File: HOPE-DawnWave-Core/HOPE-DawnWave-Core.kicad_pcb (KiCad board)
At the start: 2 copper layers, 50 parts, among them J1 USB_C_Receptacle_USB2.0_16P, J2 Screw_Terminal_01x02, SW1 RST, SW2 BOOT, U1 TLV62569DRL, U2 USBLC6-2P6, U3 ESP32-C6-WROOM-1, U4 MAX98357A, U5 BME688, X1 EYE_SPI_DISPLAY_FLIP

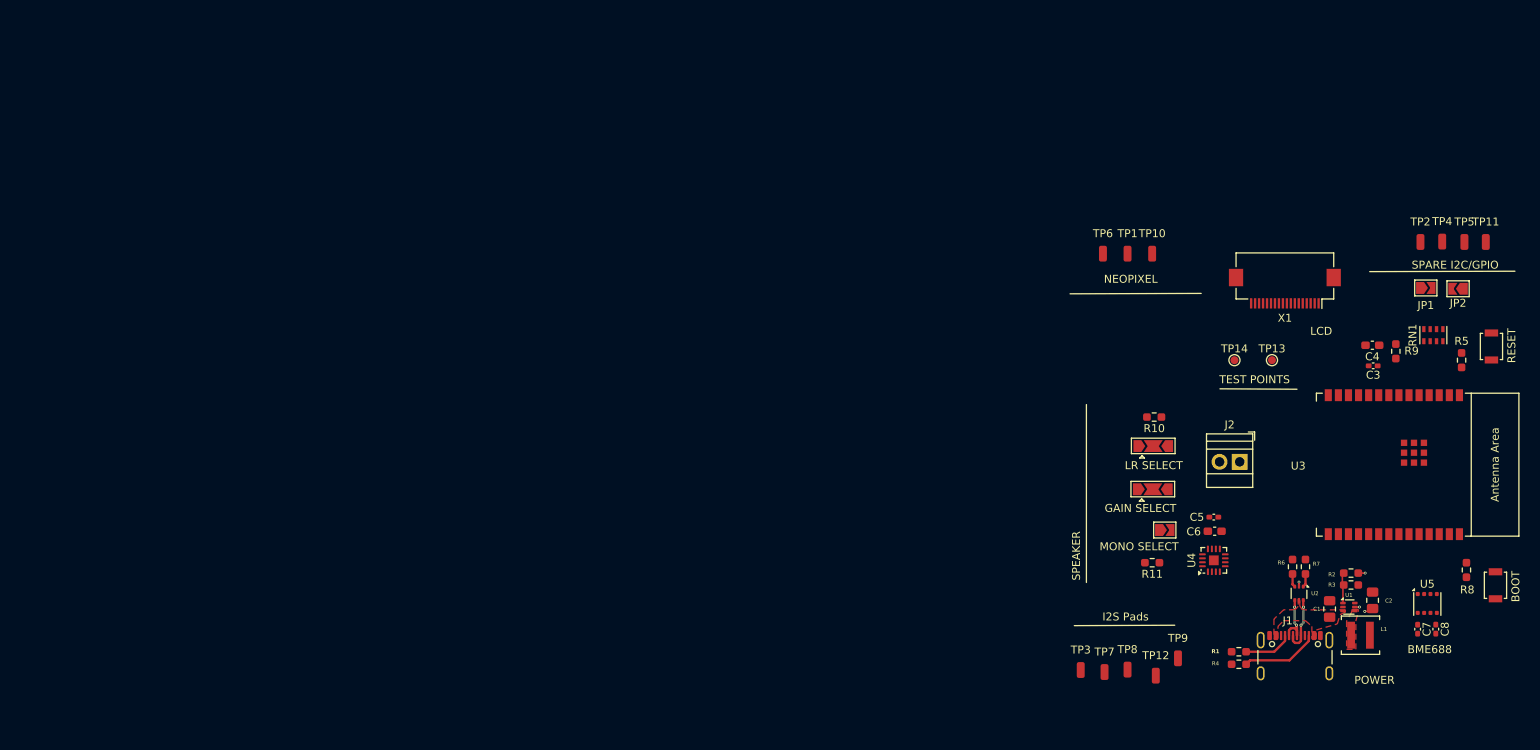
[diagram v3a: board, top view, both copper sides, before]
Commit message: fixed gitignore and completed major component placement iteration
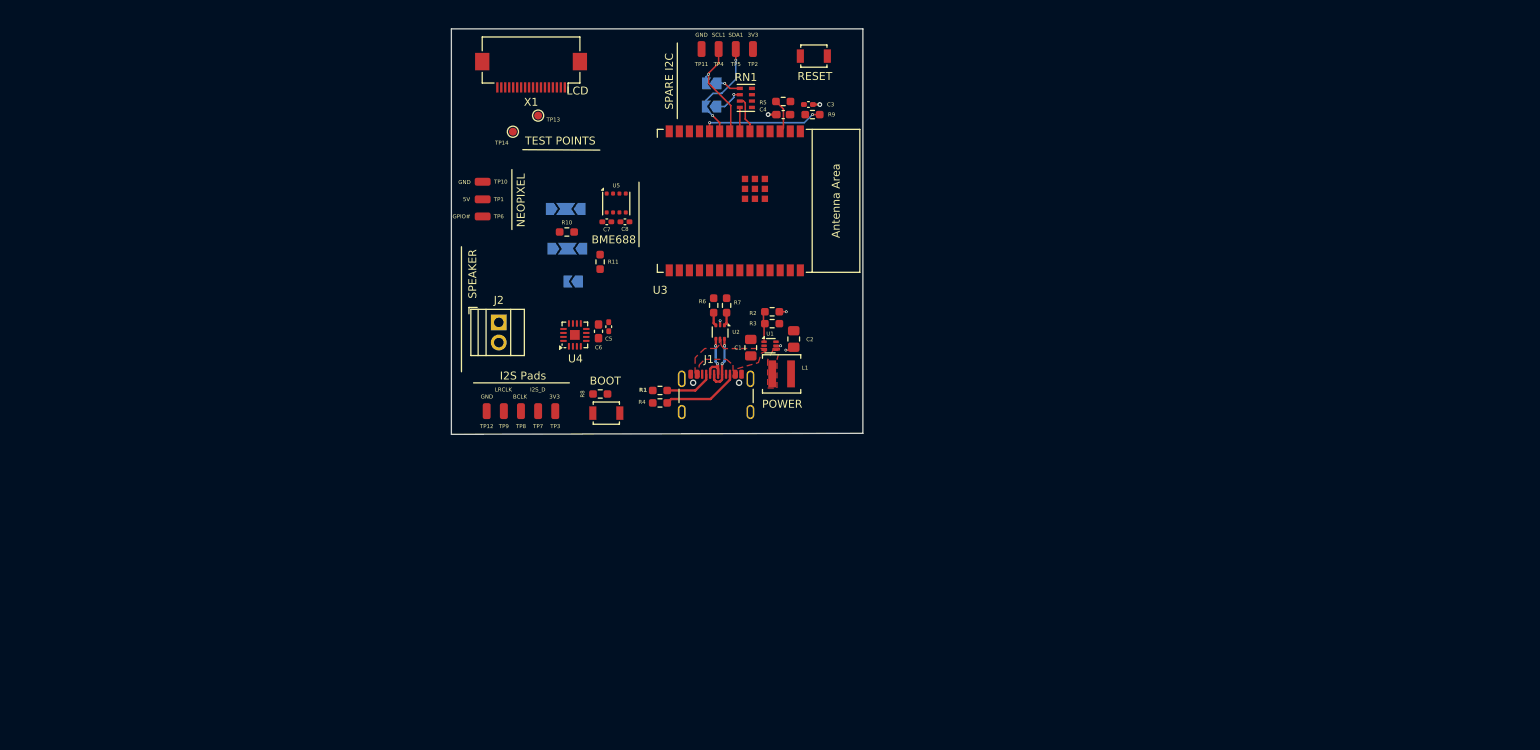
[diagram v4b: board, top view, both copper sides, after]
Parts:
- JP1, JP2, JP3, JP4, JP5: moved to B.Cu
- moved C7 114.3 mm to (142.7, 91.0), turned to 0 degrees
- moved C8 114.3 mm to (144.9, 91.0), turned to 0 degrees
- moved SW2 114.0 mm to (142.6, 115.1), turned to 180 degrees
- moved U5 113.9 mm to (143.8, 88.7)
- moved R8 111.3 mm to (141.8, 112.7), turned to 180 degrees
- moved TP11 101.7 mm to (154.6, 69.3)
- moved X1 98.7 mm to (133.1, 72.3)
- moved TP13 97.4 mm to (134.0, 77.7)
- moved JP2 96.8 mm to (155.9, 76.5)
- moved TP14 95.3 mm to (130.8, 79.7)
- moved J2 94.9 mm to (129.1, 103.7), turned to -90 degrees
- moved TP5 94.9 mm to (158.9, 69.3)
- moved TP4 94.3 mm to (156.7, 69.3)
- moved JP1 93.5 mm to (155.9, 73.6), turned to 180 degrees
- moved SW1 92.8 mm to (168.7, 70.2), turned to 180 degrees
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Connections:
- U3 pad 6: MCU_SDA0 -> MCU_SCL0
- U3 pad 7: MCU_SCL0 -> MCU_SDA0
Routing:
- net Net-(U3-GPIO8): track 0.00 -> 15.4 mm, vias 0 -> 2
- net MCU_SCL1: track 0.00 -> 13.4 mm, vias 0 -> 1
- net MCU_SDA1: track 0.00 -> 13.3 mm, vias 0 -> 2
- net MCU_SCL0: track 0.00 -> 4.60 mm
- net /MCU_EN: track 0.00 -> 4.32 mm
- net Net-(JP2-A): track 0.00 -> 3.70 mm, vias 0 -> 1
- net Net-(JP1-A): track 0.00 -> 3.42 mm, vias 0 -> 1
- net MCU_SDA0: track 0.00 -> 3.01 mm
- net GND: track 0.50 -> 2.41 mm, vias 1 -> 3
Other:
- board outline added: 51.8 x 51.1 mm
- board text added: "3V3"
- board text added: "5V"
- board text added: "BCLK"
- board text added: "GND"
- board text added: "GPIO#"
- board text added: "I2S_D"
- board text added: "LRCLK"
- board text added: "SCL1"
- board text added: "SDA1"
- board text added: "SPARE I2C"
- board text removed: "SPARE I2C/GPIO"

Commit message: big progress oops
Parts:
- moved SW1 37.4 mm to (165.9, 107.4)
- moved R5 29.0 mm to (165.1, 104.9), turned to 0 degrees
- moved R8 23.1 mm to (164.9, 112.8)
- moved SW2 23.1 mm to (165.7, 115.2)
- moved JP4 11.5 mm to (129.9, 98.0)
- moved R1 10.7 mm to (159.3, 116.3), turned to 0 degrees
- moved JP5 10.2 mm to (129.5, 93.5)
- moved JP3 10.2 mm to (128.8, 89.4)
- moved R10 10.2 mm to (128.7, 87.3)
- moved R4 9.97 mm to (159.3, 114.8), turned to 0 degrees
- moved TP1 9.85 mm to (126.7, 98.0)
- moved R11 8.54 mm to (133.9, 93.0)
- moved TP13 8.06 mm to (134.0, 85.7)
- moved U5 7.83 mm to (136.0, 88.9), turned to 90 degrees
- moved C8 7.32 mm to (138.4, 87.8), turned to 90 degrees
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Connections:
- U3 pad 11: MCU_DRST -> MCU_TD
- U3 pad 12: MCU_TD -> MCU_BACKLIGHT
- U3 pad 16: MCU_MISO -> MCU_LRCLK
- U3 pad 17: MCU_SCLK -> MCU_BCLK
- U3 pad 18: MCU_MOSI -> MCU_I2S_D
- U3 pad 19: MCU_D/C -> GPIO_NP
- U3 pad 23: MCU_BACKLIGHT -> MCU_DRST
- U3 pad 24: MCU_LRCLK -> MCU_MISO
- U3 pad 25: MCU_BCLK -> MCU_SCLK
- U3 pad 26: MCU_I2S_D -> MCU_MOSI
- U3 pad 27: GPIO_NP -> MCU_D/C
- U3 pad 6: MCU_SCL0 -> MCU_SDA0
- U3 pad 7: MCU_SDA0 -> MCU_SCL0
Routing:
- net MCU_SDA0: track 3.01 -> 41.4 mm
- net MCU_SCL0: track 4.60 -> 40.1 mm
- net /MCU_BOOT: track 0.00 -> 32.2 mm
- net MCU_LRCLK: track 0.00 -> 30.9 mm, vias 0 -> 2
- net MCU_BCLK: track 0.00 -> 30.7 mm, vias 0 -> 2
- net /MCU_USB_D-: track 0.00 -> 30.5 mm, vias 0 -> 2
- net MCU_I2S_D: track 0.00 -> 30.0 mm, vias 0 -> 2
- net /MCU_USB_D+: track 0.00 -> 28.9 mm, vias 0 -> 2
- net MCU_TD: track 0.00 -> 25.5 mm
- net GPIO_NP: track 0.00 -> 24.7 mm
- net /MCU_EN: track 4.32 -> 28.1 mm
- net MCU_BACKLIGHT: track 0.00 -> 14.7 mm
- net VBUS: track 0.58 -> 9.51 mm, vias 1 -> 2
- net GND: track 2.41 -> 11.1 mm, vias 3 -> 9
- net +3.3V: track 2.01 -> 9.55 mm, vias 2 -> 10
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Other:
- board size 51.8 x 51.1 mm -> 44.6 x 48 mm
- board text added: "+"
- board text added: "-"
- board text added: "SCL0"
- board text added: "SCL1_PU"
- board text added: "SDA0"
- board text added: "SDA1_PU"
- board text removed: "TEST POINTS"

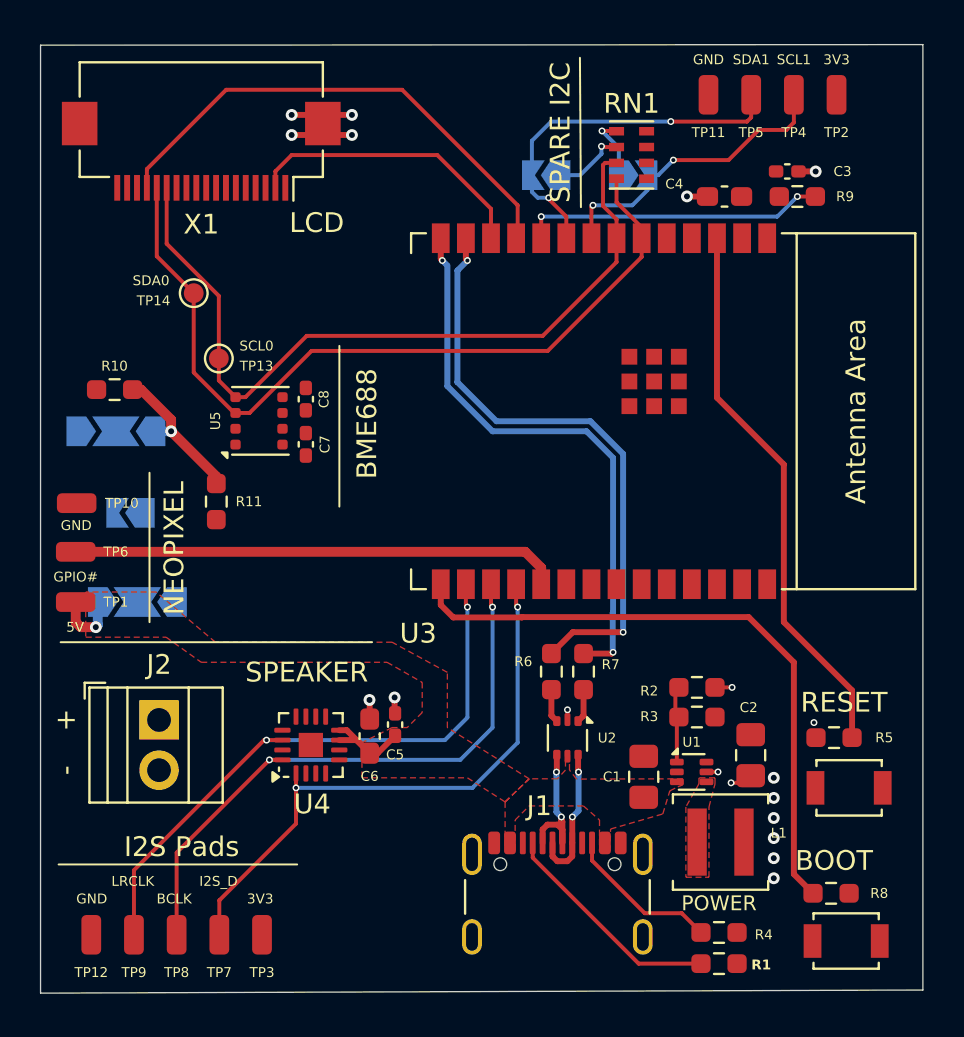
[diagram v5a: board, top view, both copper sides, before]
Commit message: Initial layout, need to resolve errors
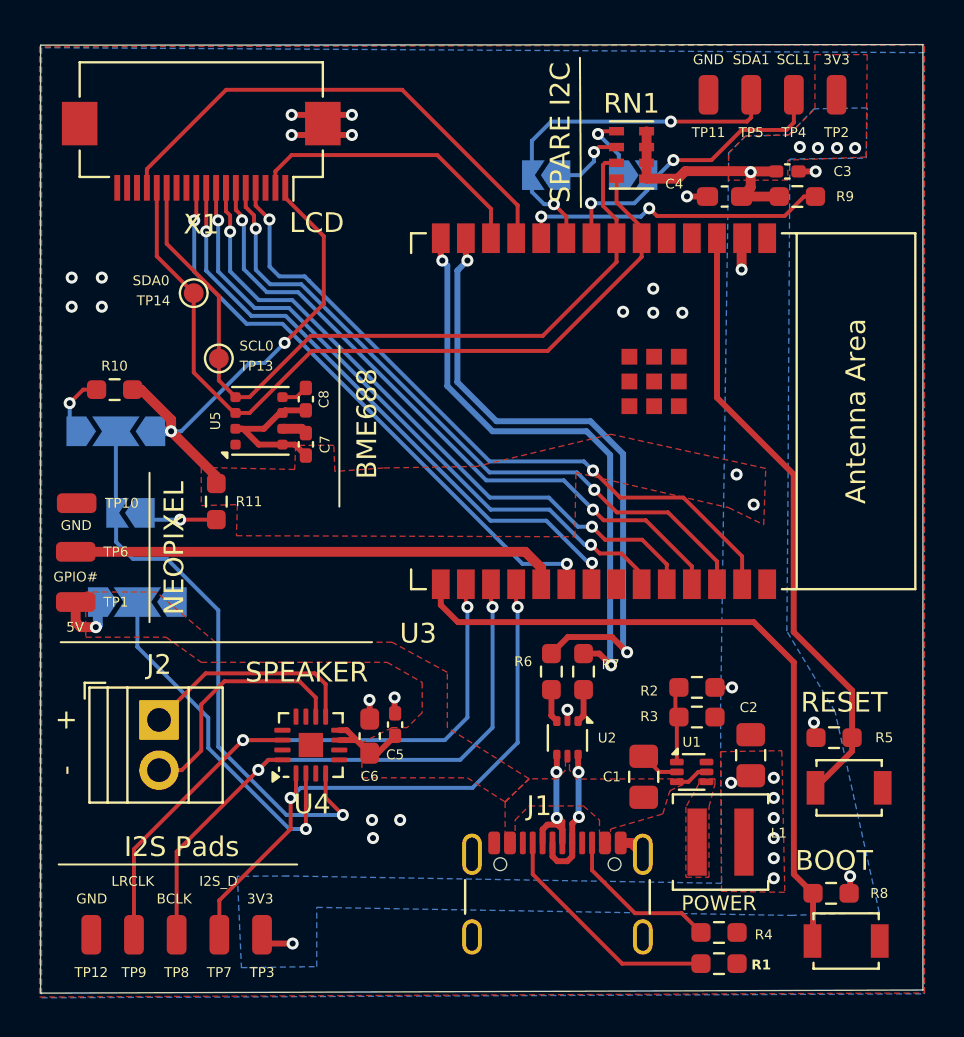
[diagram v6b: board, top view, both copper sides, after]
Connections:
- U3 pad 24: MCU_MISO -> MCU_D/C
- U3 pad 25: MCU_SCLK -> MCU_MISO
- U3 pad 27: MCU_D/C -> MCU_SCLK
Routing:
- net +3.3V: track 9.55 -> 52.2 mm, vias 10 -> 21
- net MCU_SCLK: track 0.00 -> 35.7 mm, vias 0 -> 2
- net MCU_MOSI: track 0.00 -> 34.9 mm, vias 0 -> 2
- net MCU_MISO: track 0.00 -> 34.2 mm, vias 0 -> 2
- net MCU_D/C: track 0.00 -> 33.5 mm, vias 0 -> 2
- net MCU_DRST: track 0.00 -> 32.6 mm, vias 0 -> 2
- net MCU_DISP_SEL: track 0.00 -> 31.0 mm, vias 0 -> 2
- net MCU_SD_SEL: track 0.00 -> 30.3 mm, vias 0 -> 2
- net Net-(JP3-C): track 0.00 -> 29.3 mm, vias 0 -> 1
- net Net-(JP4-C): track 0.00 -> 18.3 mm, vias 0 -> 1
- net /MAX98357A_I2S/Speaker_N: track 0.00 -> 12.5 mm
- net /MAX98357A_I2S/Speaker_P: track 0.00 -> 11.3 mm
- net GND: track 11.1 -> 17.1 mm, vias 9 -> 20
- net Net-(JP5-A): track 0.00 -> 3.76 mm, vias 0 -> 1
- net /MCU_EN: track 28.1 -> 31.4 mm
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- added copper zone on B.Cu, net +3.3V
- added copper zone on F.Cu, net +3.3V
- added copper zone on B.Cu, net GND
- added copper zone on F.Cu, net GND

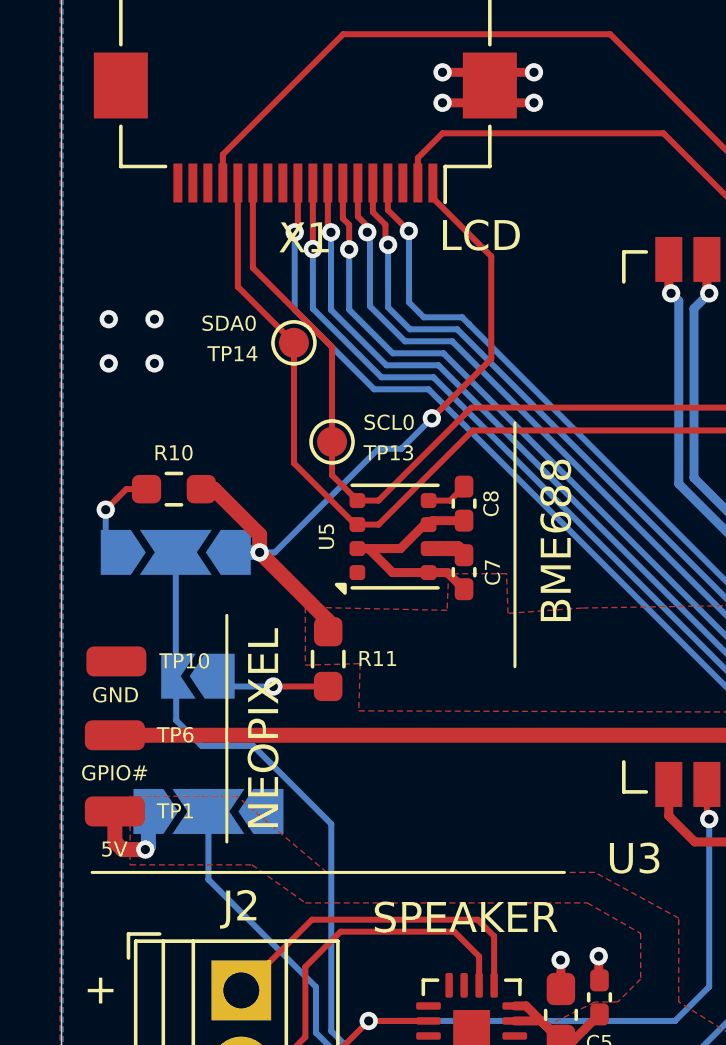
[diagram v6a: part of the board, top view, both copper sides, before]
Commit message: fixed 2 fixable drc errors - thermal reliefs
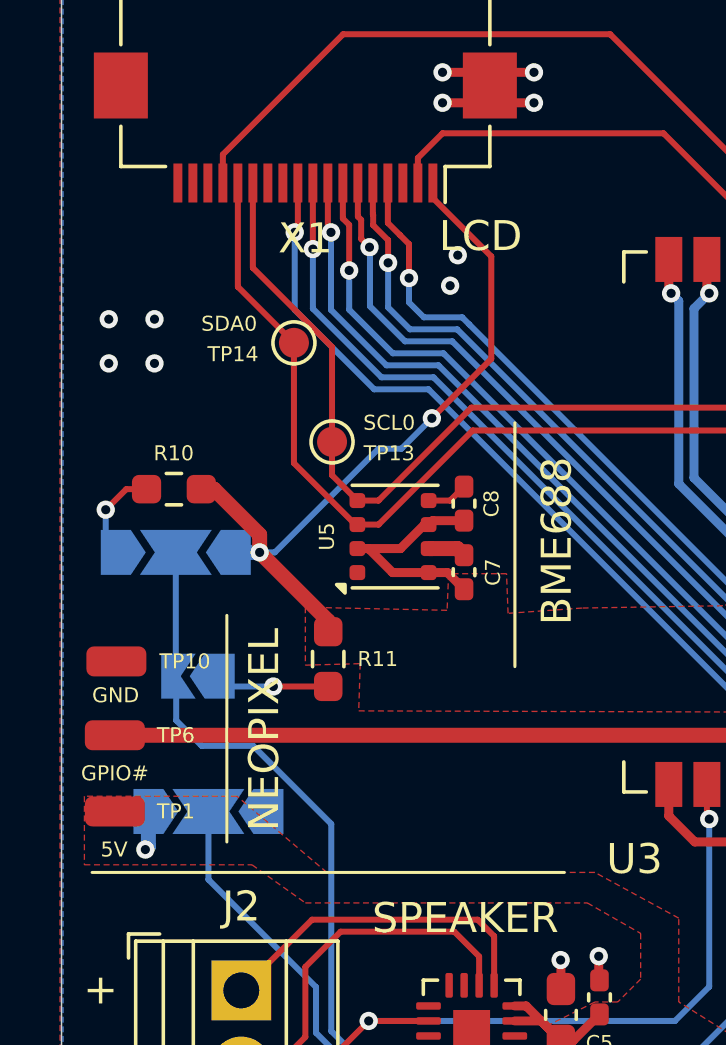
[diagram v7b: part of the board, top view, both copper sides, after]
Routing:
- net VBUS: track 10.6 -> 8.50 mm
- net GND: vias 20 -> 22

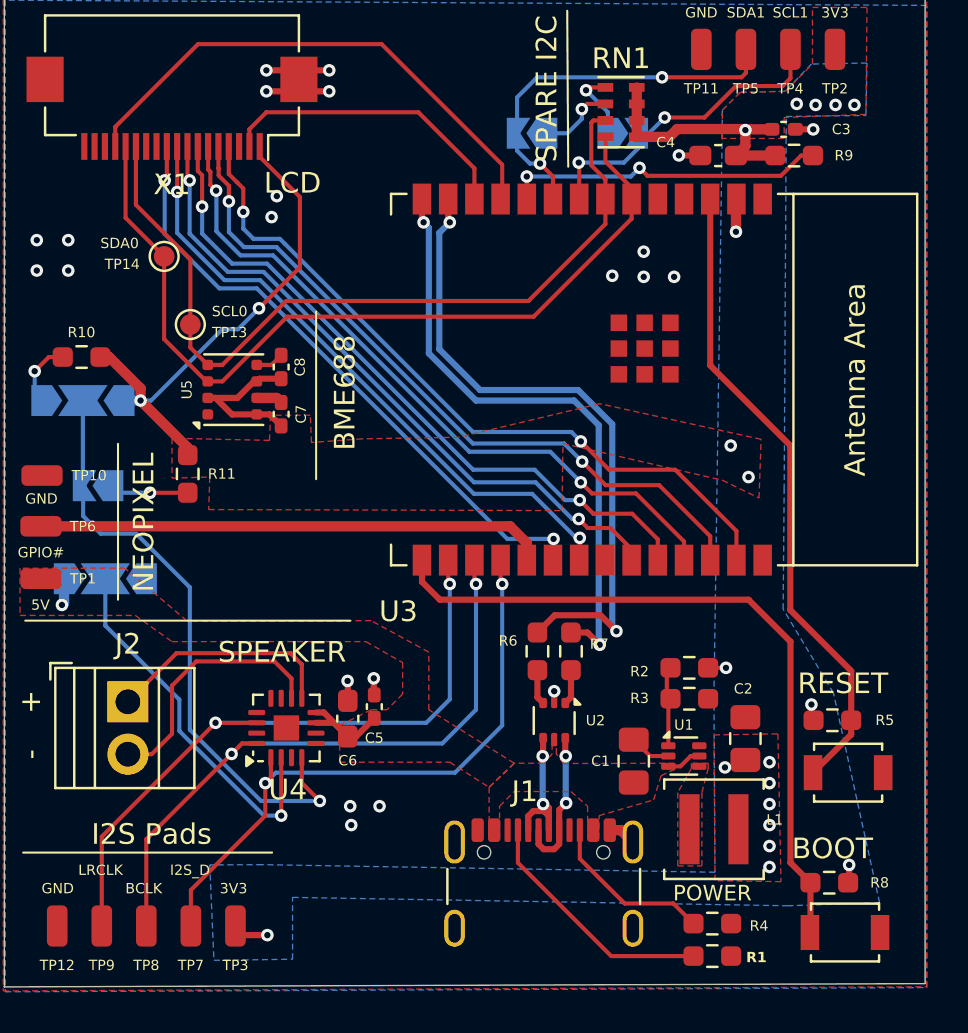
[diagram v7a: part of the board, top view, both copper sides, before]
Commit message: moved vias to fix via in pad stuff
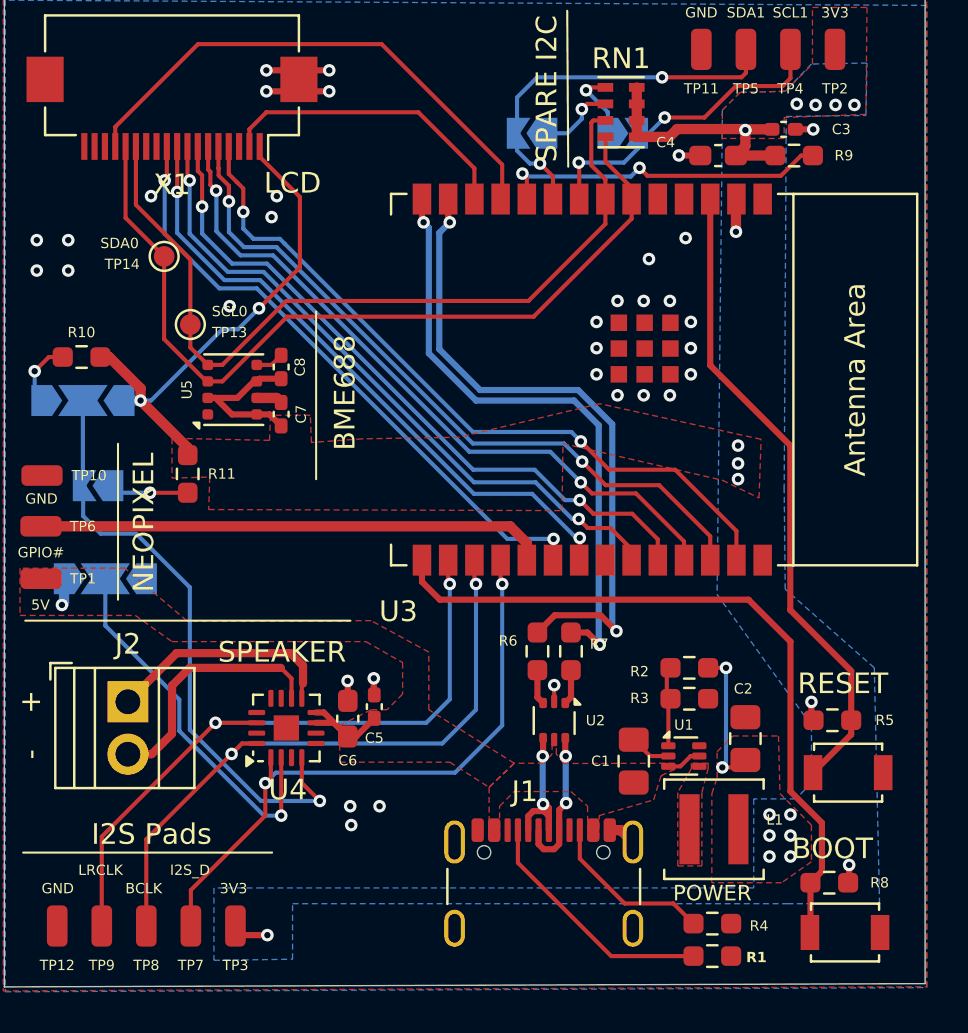
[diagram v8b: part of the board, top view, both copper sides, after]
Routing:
- net +3.3V: track 52.2 -> 57.4 mm, vias 21 -> 22
- net Net-(U3-GPIO8): track 15.7 -> 16.2 mm
- net GND: track 17.1 -> 17.4 mm, vias 22 -> 34
